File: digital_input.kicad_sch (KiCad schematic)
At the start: 8 parts, among them J10 Conn_Coaxial, U2 74LVC1G17

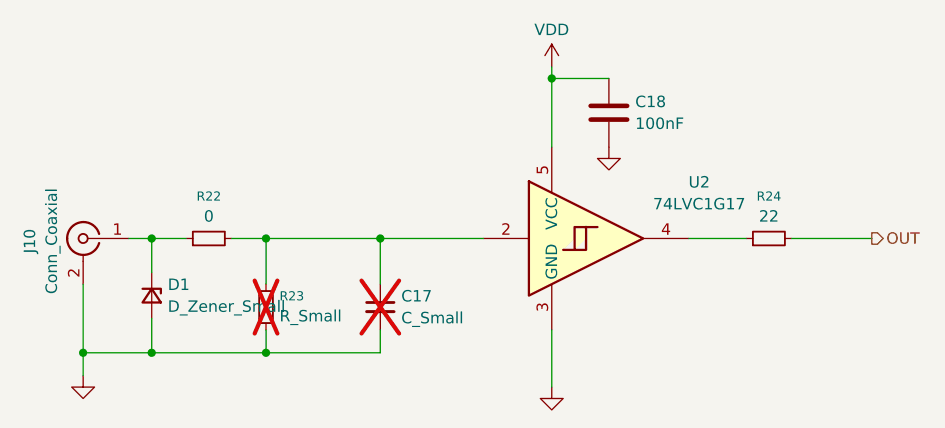
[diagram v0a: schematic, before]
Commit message: adding subproject, breakout board for nucleo
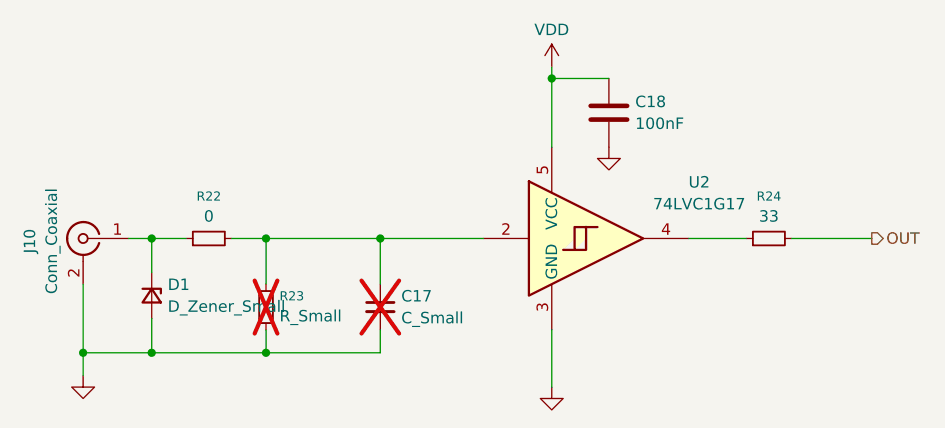
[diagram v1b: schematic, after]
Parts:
- R24: value 22 -> 33
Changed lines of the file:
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@@
 			)
 		)
-		(property "Value" "22"
+		(property "Value" "33"
 			(at 181.61 96.6032 90)
 			(effects
